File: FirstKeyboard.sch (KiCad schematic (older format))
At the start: 12 parts

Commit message: added reset switch
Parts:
- added R?: 10k, symbol Device:R_Small
- added SW?: SW_Push, symbol Switch:SW_Push
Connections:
- wire segments 37 -> 42
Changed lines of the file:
@@
 	2750 2850 2550 2850
 Connection ~ 2550 2850
+$Comp
+L Switch:SW_Push SW?
+U 1 1 5E8AC1BD
+P 2900 2350
+F 0 "SW?" H 2900 2635 50  0000 C CNN
+F 1 "SW_Push" H 2900 2544 50  0000 C CNN
+F 2 "" H 2900 2550 50  0001 C CNN
+F 3 "~" H 2900 2550 50  0001 C CNN
+	1    2900 2350
+	1    0    0    -1
+$EndComp
+$Comp
+L power:GND #PWR?
+U 1 1 5E8ACDF4
+P 2600 2250
+F 0 "#PWR?" H 2600 2000 50  0001 C CNN
+F 1 "GND" H 2605 2077 50  0000 C CNN
+F 2 "" H 2600 2250 50  0001 C CNN
+F 3 "" H 2600 2250 50  0001 C CNN
+	1    2600 2250
+	1    0    0    -1
+$EndComp
+$Comp
+L power:+5V #PWR?
+U 1 1 5E8AD7EF
+P 3150 1850
+F 0 "#PWR?" H 3150 1700 50  0001 C CNN
+F 1 "+5V" H 3165 2023 50  0000 C CNN
+F 2 "" H 3150 1850 50  0001 C CNN
+F 3 "" H 3150 1850 50  0001 C CNN
+	1    3150 1850
+	1    0    0    -1
+$EndComp
+$Comp
+L Device:R_Small R?
+U 1 1 5E8AE14B
+P 3150 2050
+F 0 "R?" H 3209 2096 50  0000 L CNN
+F 1 "10k" H 3209 2005 50  0000 L CNN
+F 2 "" H 3150 2050 50  0001 C CNN
+F 3 "~" H 3150 2050 50  0001 C CNN
+	1    3150 2050
+	1    0    0    -1
+$EndComp
+Wire Wire Line
+	3200 2350 3150 2350
+Wire Wire Line
+	3150 2150 3150 2350
+Connection ~ 3150 2350
+Wire Wire Line
+	3150 2350 3100 2350
+Wire Wire Line
+	2700 2350 2700 2250
+Wire Wire Line
+	2700 2250 2600 2250
 $EndSCHEMATC

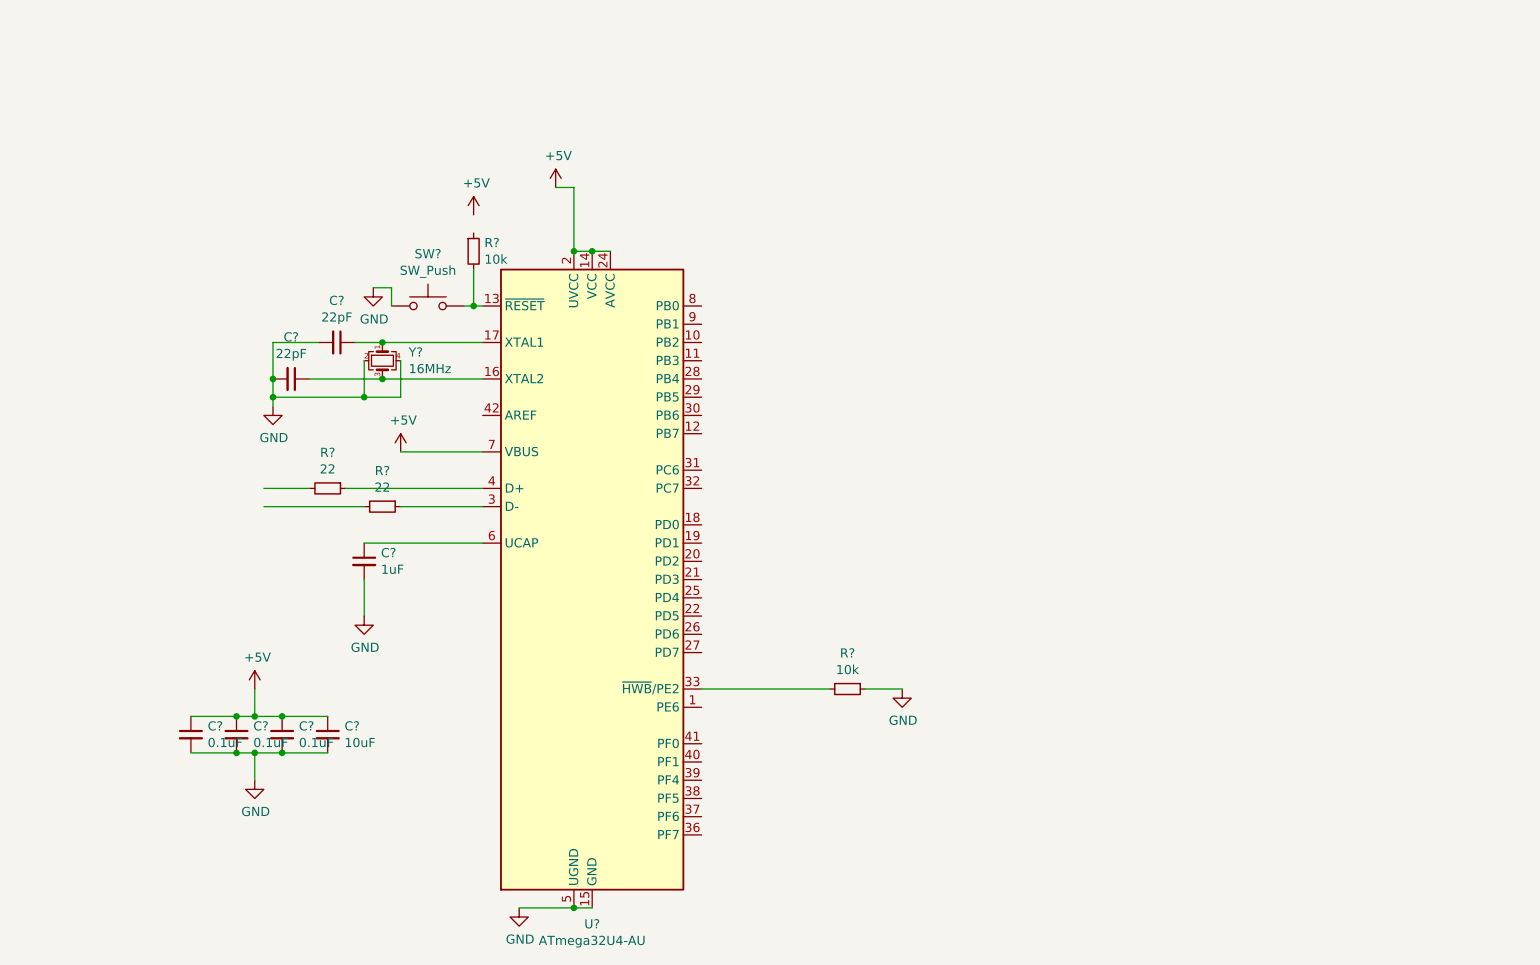
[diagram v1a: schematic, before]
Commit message: Added switch matrix, and doubled it
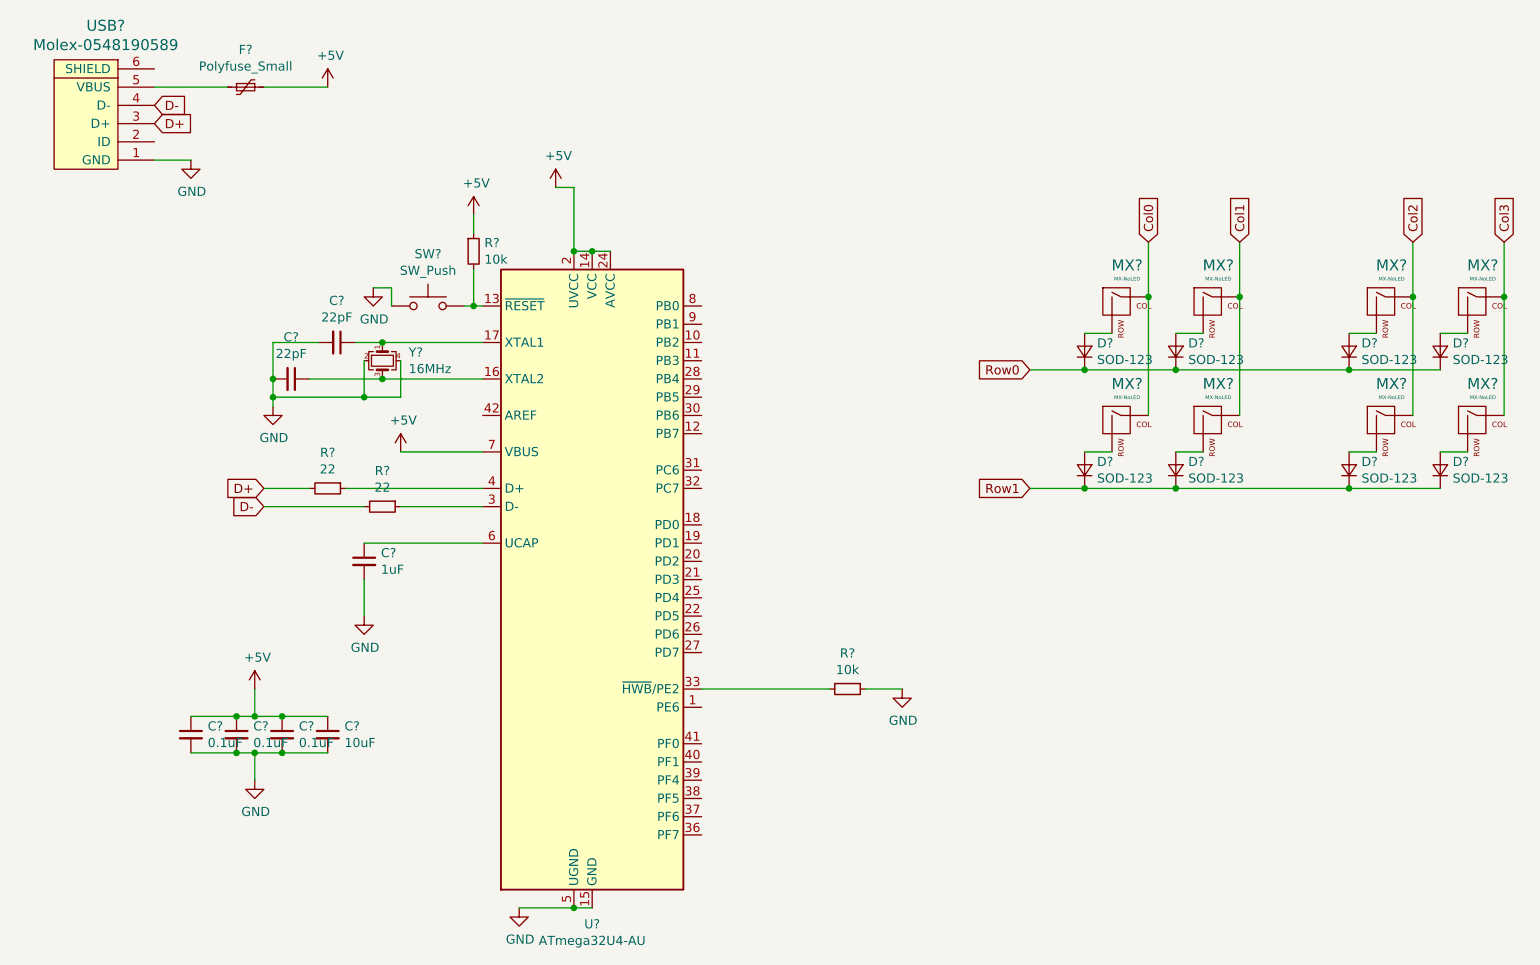
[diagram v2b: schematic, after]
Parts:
- added D? (x8): SOD-123, symbol Device:D_Small
- added F?: Polyfuse_Small, symbol Device:Polyfuse_Small
- added MX? (x8): MX-NoLED, symbol MX_Alps_Hybrid:MX-NoLED
- added USB?: Molex-0548190589, symbol random-keyboard-parts:Molex-0548190589
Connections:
- net labels added: Col0, Col1, Col2, Col3, D+, D-, Row0, Row1
- wire segments 42 -> 70
